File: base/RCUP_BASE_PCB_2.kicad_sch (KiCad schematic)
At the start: 34 parts, among them U1 UA741CP, U5 BNO055

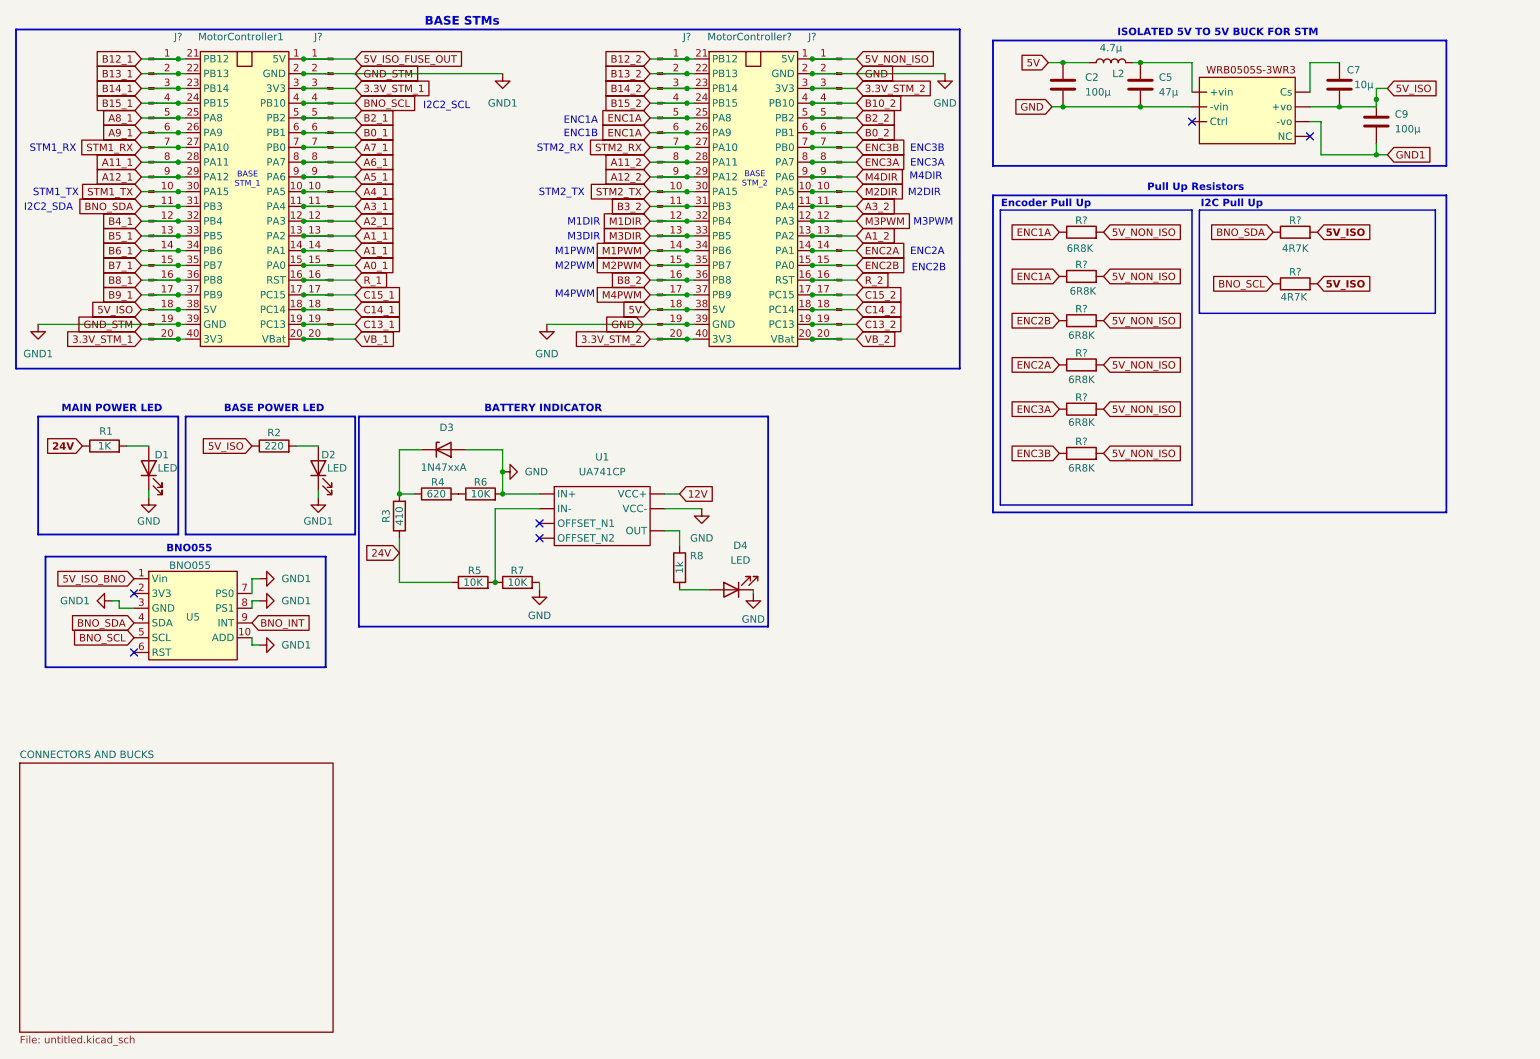
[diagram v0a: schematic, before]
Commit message: changed the whole schematic and organised it
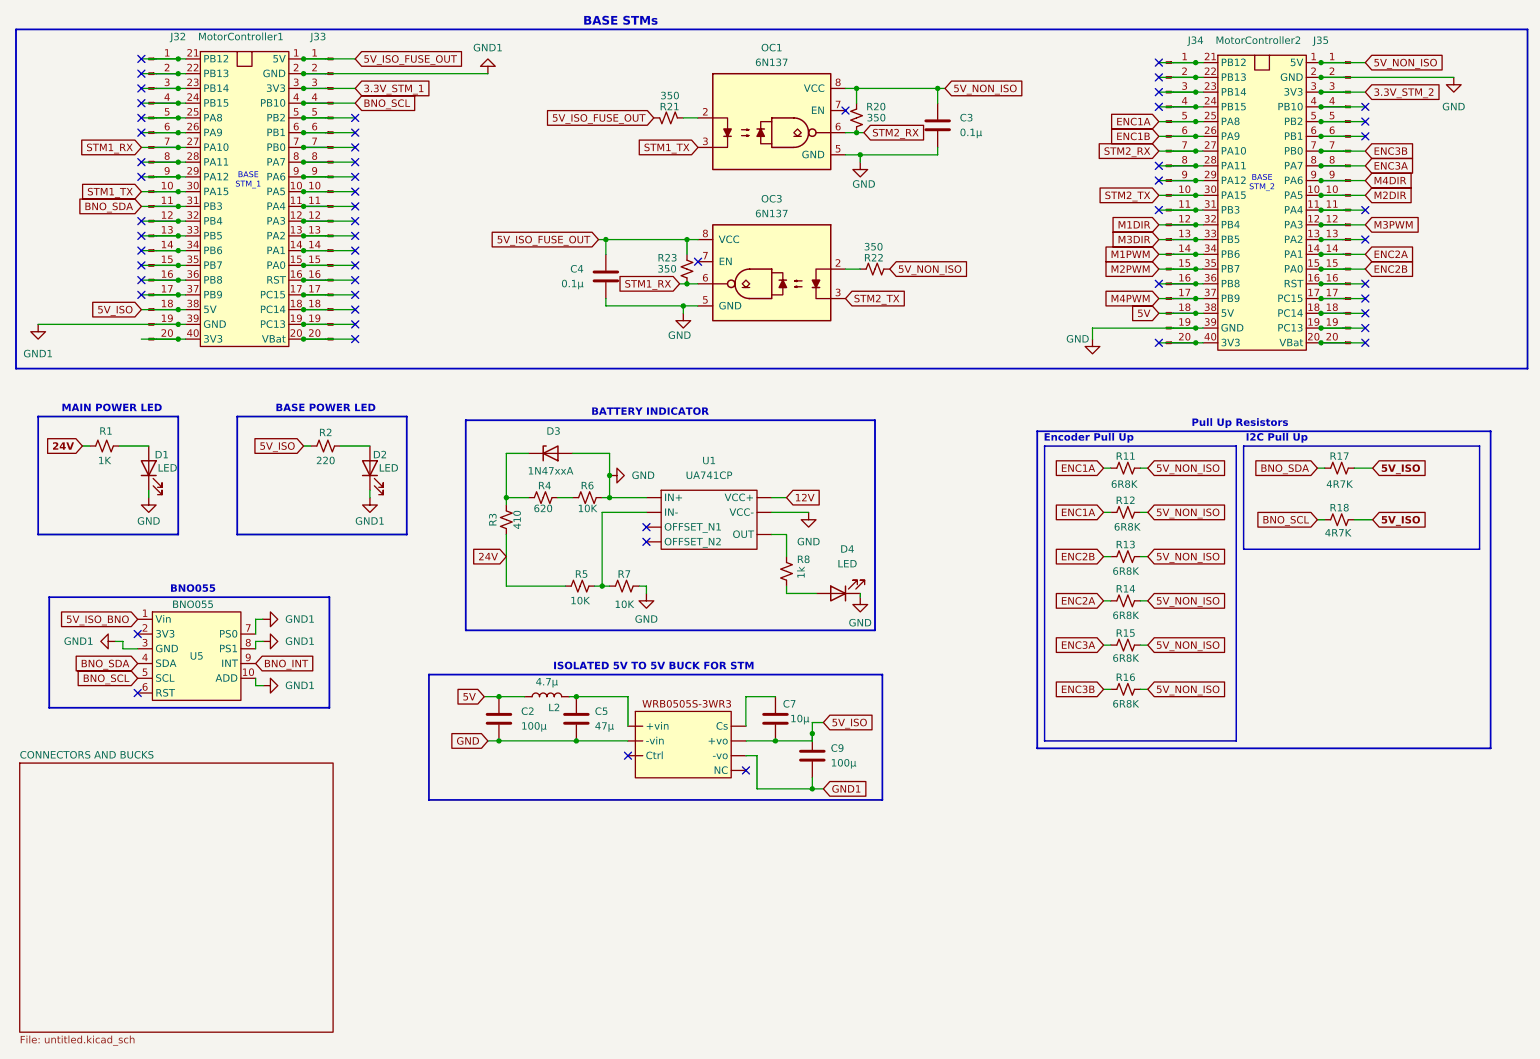
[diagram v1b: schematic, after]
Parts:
- added C3, C4: 0.1µ, symbol Device:C
- added OC1, OC3: 6N137, PCM_Package_DIP_AKL:DIP-8_W7.62mm_LongPads, symbol PCM_Optocoupler_Logic_AKL:6N137
- added R20, R21, R22, R23: 350, symbol Device:R_Small_US
- R1, R2, R3, R4, R5, R6, R7, R8: symbol Device:R -> Device:R_Small_US
- R11, R12, R13, R14, R15, R16, R17, R18: renamed from R?; symbol Device:R -> Device:R_Small_US
- gave numbers to parts that had none: 5
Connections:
- net 3.3V_STM_1: no longer J32.20 (Pin_20), MotorController1.40 (3V3)
- net 3.3V_STM_2: no longer J34.20 (Pin_20), MotorController2.40 (3V3)
- net 5V_ISO_FUSE_OUT: now also C4.1, OC3.8 (VCC), R21.1, R23.1
- net 5V_NON_ISO: now also C3.1, OC1.8 (VCC), R20.1, R22.1
- net ENC1A: no longer J34.6 (Pin_6), MotorController2.26 (PA9)
- net GND: now also C3.2, C4.2, OC1.5 (GND), OC3.5 (GND)
- net STM1_RX: now also OC3.6, R23.2
- net STM1_TX: now also OC1.3
- net STM2_RX: now also OC1.6, R20.2
- net STM2_TX: now also OC3.3
- net A0_1: no longer names the net of J33.15 (Pin_15), MotorController1.15 (PA0)
- net A11_1: no longer names the net of J32.8 (Pin_8), MotorController1.28 (PA11)
- net A11_2: no longer names the net of J34.8 (Pin_8), MotorController2.28 (PA11)
- net A12_1: no longer names the net of J32.9 (Pin_9), MotorController1.29 (PA12)
- net A12_2: no longer names the net of J34.9 (Pin_9), MotorController2.29 (PA12)
- net A1_1: no longer names the net of J33.13 (Pin_13), MotorController1.13 (PA2)
- net A1_1: no longer J33.14 (Pin_14), MotorController1.14 (PA1)
- net A1_2: no longer names the net of J35.13 (Pin_13), MotorController2.13 (PA2)
- net A2_1: no longer names the net of J33.12 (Pin_12), MotorController1.12 (PA3)
- net A3_1: no longer names the net of J33.11 (Pin_11), MotorController1.11 (PA4)
- net A3_2: no longer names the net of J35.11 (Pin_11), MotorController2.11 (PA4)
- net A4_1: no longer names the net of J33.10 (Pin_10), MotorController1.10 (PA5)
- net A5_1: no longer names the net of J33.9 (Pin_9), MotorController1.9 (PA6)
- net A6_1: no longer names the net of J33.8 (Pin_8), MotorController1.8 (PA7)
- net A7_1: no longer names the net of J33.7 (Pin_7), MotorController1.7 (PB0)
- net A8_1: no longer names the net of J32.5 (Pin_5), MotorController1.25 (PA8)
- net A9_1: no longer names the net of J32.6 (Pin_6), MotorController1.26 (PA9)
- net B0_1: no longer names the net of J33.6 (Pin_6), MotorController1.6 (PB1)
- net B0_2: no longer names the net of J35.6 (Pin_6), MotorController2.6 (PB1)
- net B10_2: no longer names the net of J35.4 (Pin_4), MotorController2.4 (PB10)
- net B12_1: no longer names the net of J32.1 (Pin_1), MotorController1.21 (PB12)
- net B12_2: no longer names the net of J34.1 (Pin_1), MotorController2.21 (PB12)
- net B13_1: no longer names the net of J32.2 (Pin_2), MotorController1.22 (PB13)
- net B13_2: no longer names the net of J34.2 (Pin_2), MotorController2.22 (PB13)
- net B14_1: no longer names the net of J32.3 (Pin_3), MotorController1.23 (PB14)
- net B14_2: no longer names the net of J34.3 (Pin_3), MotorController2.23 (PB14)
- net B15_1: no longer names the net of J32.4 (Pin_4), MotorController1.24 (PB15)
- net B15_2: no longer names the net of J34.4 (Pin_4), MotorController2.24 (PB15)
- net B2_1: no longer names the net of J33.5 (Pin_5), MotorController1.5 (PB2)
- net B2_2: no longer names the net of J35.5 (Pin_5), MotorController2.5 (PB2)
- net B3_2: no longer names the net of J34.11 (Pin_11), MotorController2.31 (PB3)
- net B4_1: no longer names the net of J32.12 (Pin_12), MotorController1.32 (PB4)
- net B5_1: no longer names the net of J32.13 (Pin_13), MotorController1.33 (PB5)
- net B6_1: no longer names the net of J32.14 (Pin_14), MotorController1.34 (PB6)
- net B7_1: no longer names the net of J32.15 (Pin_15), MotorController1.35 (PB7)
- net B8_1: no longer names the net of J32.16 (Pin_16), MotorController1.36 (PB8)
- net B8_2: no longer names the net of J34.16 (Pin_16), MotorController2.36 (PB8)
- net B9_1: no longer names the net of J32.17 (Pin_17), MotorController1.37 (PB9)
- net C13_1: no longer names the net of J33.19 (Pin_19), MotorController1.19 (PC13)
- net C13_2: no longer names the net of J35.19 (Pin_19), MotorController2.19 (PC13)
- net C14_1: no longer names the net of J33.18 (Pin_18), MotorController1.18 (PC14)
- net C14_2: no longer names the net of J35.18 (Pin_18), MotorController2.18 (PC14)
- net C15_1: no longer names the net of J33.17 (Pin_17), MotorController1.17 (PC15)
- net C15_2: no longer names the net of J35.17 (Pin_17), MotorController2.17 (PC15)
- net R_1: no longer names the net of J33.16 (Pin_16), MotorController1.16 (RST)
- net R_2: no longer names the net of J35.16 (Pin_16), MotorController2.16 (RST)
- net VB_1: no longer names the net of J33.20 (Pin_20), MotorController1.20 (VBat)
- net VB_2: no longer names the net of J35.20 (Pin_20), MotorController2.20 (VBat)
- new net: OC3.2, R22.2
- new net: J34.20 (Pin_20), MotorController2.40 (3V3)
- new net: J33.14 (Pin_14), MotorController1.14 (PA1)
- new net: OC1.2, R21.2
- new net: J32.20 (Pin_20), MotorController1.40 (3V3)
- new net ENC1B: J34.6 (Pin_6), MotorController2.26 (PA9)
- no-connect marks 6 -> 57
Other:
- note removed: "ENC1A"
- note removed: "ENC1B"
- note removed: "ENC2A"
- note removed: "ENC2B"
- note removed: "ENC3A"
- note removed: "ENC3B"
- note removed: "I2C2_SCL"
- note removed: "I2C2_SDA"
- note removed: "M1DIR"
- note removed: "M1PWM"
- note removed: "M2DIR"
- note removed: "M2PWM"
- note removed: "M3DIR"
- note removed: "M3PWM"
- note removed: "M4DIR"
- note removed: "M4PWM"
- note removed: "STM1_RX"
- note removed: "STM1_TX"
- note removed: "STM2_RX"
- note removed: "STM2_TX"
- moved on the sheet: C2, C5, C7, C9, D2, D3, D4, J34, J35, L2, MotorController2, U1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

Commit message: components placed\
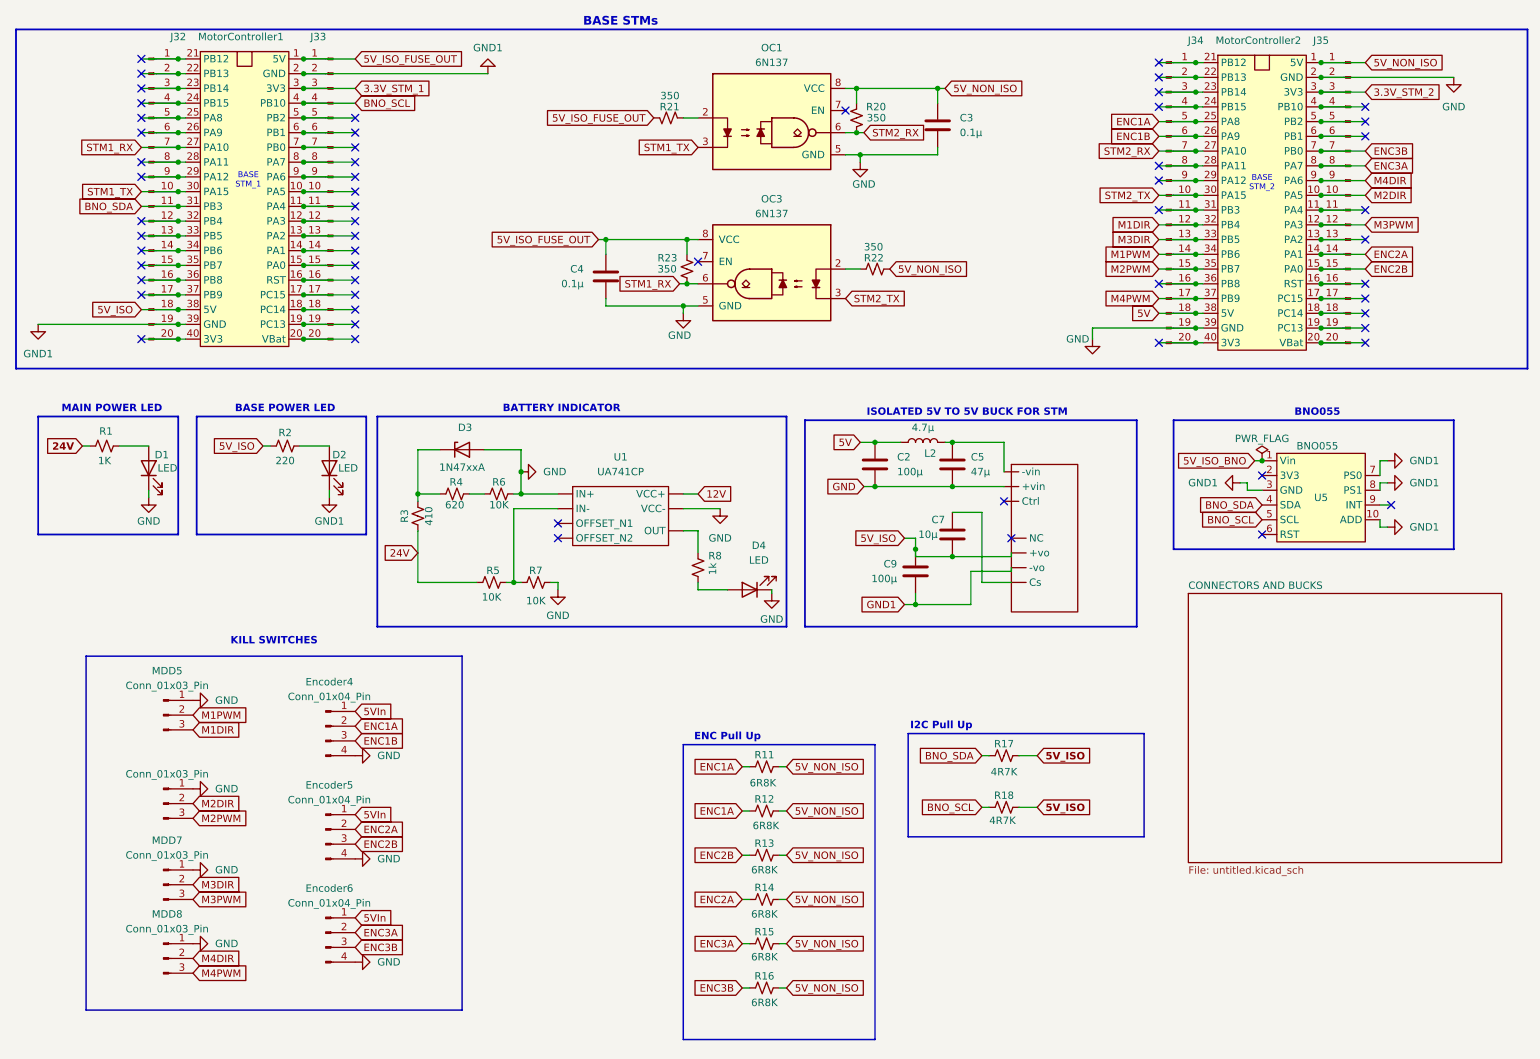
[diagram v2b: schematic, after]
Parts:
- added Encoder4, Encoder5, Encoder6: Conn_01x04_Pin, Connector_JST:JST_XH_B4B-XH-A_1x04_P2.50mm_Vertical, symbol Connector:Conn_01x04_Pin
- added MDD5, MDD6, MDD7, MDD8: Conn_01x03_Pin, Connector_JST:JST_XH_B3B-XH-A_1x03_P2.50mm_Vertical, symbol Connector:Conn_01x03_Pin
- C3, C4: footprint (none) -> Capacitor_SMD:C_0201_0603Metric
- D1, D2, D4: footprint (none) -> LED_SMD:LED_0201_0603Metric
- J32, J33, J34, J35: footprint (none) -> Connector_PinHeader_2.54mm:PinHeader_1x20_P2.54mm_Vertical_SMD_Pin1Left
- R1, R11, R12, R13, R14, R15, R16, R17, R18, R2, R20, R21, R22, R23, R3, R4, R5, R6, R7, R8: footprint (none) -> PCM_4ms_Resistor:R_0603
- U1: footprint (none) -> UA741CP:DIP794W45P254L959H508Q8
- U5: footprint RM_footprintss:BNO055_7Semi -> ROBO:7_semi_BNO055
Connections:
- net ENC1A: now also Encoder4.2 (Pin_2)
- net ENC1B: now also Encoder4.3 (Pin_3)
- net ENC2A: now also Encoder5.2 (Pin_2)
- net ENC2B: now also Encoder5.3 (Pin_3)
- net ENC3A: now also Encoder6.2 (Pin_2)
- net ENC3B: now also Encoder6.3 (Pin_3)
- net GND: now also Encoder4.4 (Pin_4), Encoder5.4 (Pin_4), Encoder6.4 (Pin_4), MDD5.1 (Pin_1), MDD6.1 (Pin_1), MDD7.1 (Pin_1), MDD8.1 (Pin_1)
- net M1DIR: now also MDD5.3 (Pin_3)
- net M1PWM: now also MDD5.2 (Pin_2)
- net M2DIR: now also MDD6.2 (Pin_2)
- net M2PWM: now also MDD6.3 (Pin_3)
- net M3DIR: now also MDD7.2 (Pin_2)
- net M3PWM: now also MDD7.3 (Pin_3)
- net M4DIR: now also MDD8.2 (Pin_2)
- net M4PWM: now also MDD8.3 (Pin_3)
- net BNO_INT: no longer names the net of U5.9 (INT)
- new net 5VIn: Encoder4.1 (Pin_1), Encoder5.1 (Pin_1), Encoder6.1 (Pin_1)
- no-connect marks 57 -> 59
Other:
- note added: "ENC Pull Up"
- note added: "KILL SWITCHES"
- note removed: "Encoder Pull Up"
- note removed: "Pull Up Resistors"
- moved on the sheet: C2, C5, C7, C9, D2, D3, D4, L2, R11, R12, R13, R14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

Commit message: made the suggested changes
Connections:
- net ENC1A: no longer R12.1
- net ENC1B: now also R12.1
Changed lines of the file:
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@@
 		)
 	)
-	(global_label "ENC1A"
+	(global_label "ENC1B"
 		(shape input)
 		(at 142.875 151.765 180)
@@
 		)
 		(property "Intersheetrefs" "${INTERSHEET_REFS}"
-			(at 133.8422 151.765 0)
+			(at 133.6608 151.765 0)
 			(effects
 				(font

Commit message: 50% routing done
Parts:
- C1: renamed from C4; footprint Capacitor_SMD:C_0201_0603Metric -> Capacitor_SMD:C_0603_1608Metric_Pad1.08x0.95mm_HandSolder
- C2, C5: footprint Capacitor_SMD:C_0201_0603Metric -> Capacitor_SMD:C_0603_1608Metric_Pad1.08x0.95mm_HandSolder
- C3: renamed from C9; footprint Capacitor_SMD:C_0201_0603Metric -> Capacitor_SMD:C_0603_1608Metric_Pad1.08x0.95mm_HandSolder
- C4: renamed from C3; footprint Capacitor_SMD:C_0201_0603Metric -> Capacitor_SMD:C_0603_1608Metric_Pad1.08x0.95mm_HandSolder
- C6: renamed from C7; footprint Capacitor_SMD:C_0201_0603Metric -> Capacitor_SMD:C_0603_1608Metric_Pad1.08x0.95mm_HandSolder
- D1, D2, D4: footprint LED_SMD:LED_0201_0603Metric -> Diode_SMD:D_0805_2012Metric_Pad1.15x1.40mm_HandSolder
- R1, R11, R12, R13, R14, R15, R16, R2, R3, R4, R5, R6, R7: footprint PCM_4ms_Resistor:R_0603 -> PCM_Resistor_SMD_AKL:R_0603_1608Metric_Pad0.98x0.95mm_HandSolder
- R10: renamed from R8; footprint PCM_4ms_Resistor:R_0603 -> PCM_Resistor_SMD_AKL:R_0603_1608Metric_Pad0.98x0.95mm_HandSolder
- R17: renamed from R20; footprint PCM_4ms_Resistor:R_0603 -> PCM_Resistor_SMD_AKL:R_0603_1608Metric_Pad0.98x0.95mm_HandSolder
- R18: renamed from R22; footprint PCM_4ms_Resistor:R_0603 -> PCM_Resistor_SMD_AKL:R_0603_1608Metric_Pad0.98x0.95mm_HandSolder
- R19: renamed from R17; footprint PCM_4ms_Resistor:R_0603 -> PCM_Resistor_SMD_AKL:R_0603_1608Metric_Pad0.98x0.95mm_HandSolder
- R20: renamed from R18; footprint PCM_4ms_Resistor:R_0603 -> PCM_Resistor_SMD_AKL:R_0603_1608Metric_Pad0.98x0.95mm_HandSolder
- R8: renamed from R21; footprint PCM_4ms_Resistor:R_0603 -> PCM_Resistor_SMD_AKL:R_0603_1608Metric_Pad0.98x0.95mm_HandSolder
- R9: renamed from R23; footprint PCM_4ms_Resistor:R_0603 -> PCM_Resistor_SMD_AKL:R_0603_1608Metric_Pad0.98x0.95mm_HandSolder
- renumbered Encoder4 to Encoder1, Encoder5 to Encoder2, Encoder6 to Encoder3, J32 to J1, J33 to J2, J34 to J3, J35 to J4, L2 to L1, MDD5 to MDD1, MDD6 to MDD2, MDD7 to MDD3, MDD8 to MDD4, OC3 to OC2, U9 to U2, U5 to U3
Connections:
- net 12V: now also U1.7 (VCC+); no longer U1. (OUT)
- net 5V: now also C4.1, OC1.8 (VCC), R17.1, R18.1; no longer J3.18 (Pin_18), MotorController2.38 (5V)
- net 5V_ISO: now also U2.5 (+vo); no longer U2. (Cs)
- net 5V_NON_ISO: no longer C4.1, J4.1 (Pin_1), MotorController2.1 (5V), OC1.8 (VCC), R17.1, R18.1
- net ENC3A: now also J4.9 (Pin_9), MotorController2.9 (PA6); no longer J4.8 (Pin_8), MotorController2.8 (PA7)
- net ENC3B: now also J4.8 (Pin_8), MotorController2.8 (PA7); no longer J4.7 (Pin_7), MotorController2.7 (PB0)
- net GND: now also U1.4 (VCC-), U2.2 (-vin); no longer U1. (OUT), U2. (Cs)
- net GND1: now also U2.6 (-vo); no longer U2. (Cs)
- net M2DIR: now also J3.13 (Pin_13), MotorController2.33 (PB5); no longer J4.10 (Pin_10), MotorController2.10 (PA5)
- net M3DIR: now also J4.10 (Pin_10), MotorController2.10 (PA5); no longer J3.13 (Pin_13), MotorController2.33 (PB5)
- net M3PWM: now also J4.13 (Pin_13), MotorController2.13 (PA2); no longer J4.12 (Pin_12), MotorController2.12 (PA3)
- net M4DIR: now also J4.11 (Pin_11), MotorController2.11 (PA4); no longer J4.9 (Pin_9), MotorController2.9 (PA6)
- net at C5.1, L1.2: now also U2.1 (+vin); no longer U2. (Cs)
- net at C6.1: now also U2.7 (Cs); no longer U2. (Cs)
- net at R5.2, R7.1: now also U1.2 (IN-); no longer U1. (OUT)
- net at R10.1: now also U1.6 (OUT); no longer U1. (OUT)
- net at R4.2, R6.1: now also U1.3 (IN+)
- new net: J4.12 (Pin_12), MotorController2.12 (PA3)
- new net: J4.7 (Pin_7), MotorController2.7 (PB0)
- new net 5V_NON_ISO_IN: J3.18 (Pin_18), J4.1 (Pin_1), MotorController2.1 (5V), MotorController2.38 (5V)
- no-connect marks 59 -> 60
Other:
- sheet CONNECTORS AND BUCKS renamed p

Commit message: 1st iteration complete
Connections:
- net GND: no longer C1.2, OC2.5 (GND)
- net GND1: now also C1.2, OC2.5 (GND)
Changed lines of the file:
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@@
 			)
 		)
-		(property "Value" "GND"
+		(property "Value" "GND1"
 			(at 132.08 69.85 0)
 			(effects
